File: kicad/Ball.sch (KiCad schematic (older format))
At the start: 32 parts, among them J901 power, K301 G5V-1, Q301 BC547, Q302 BC547, Q303 BC557, Q304 2N3819, Q305 BC547, Q306 2N3819, U301 TL082, U302 TL082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

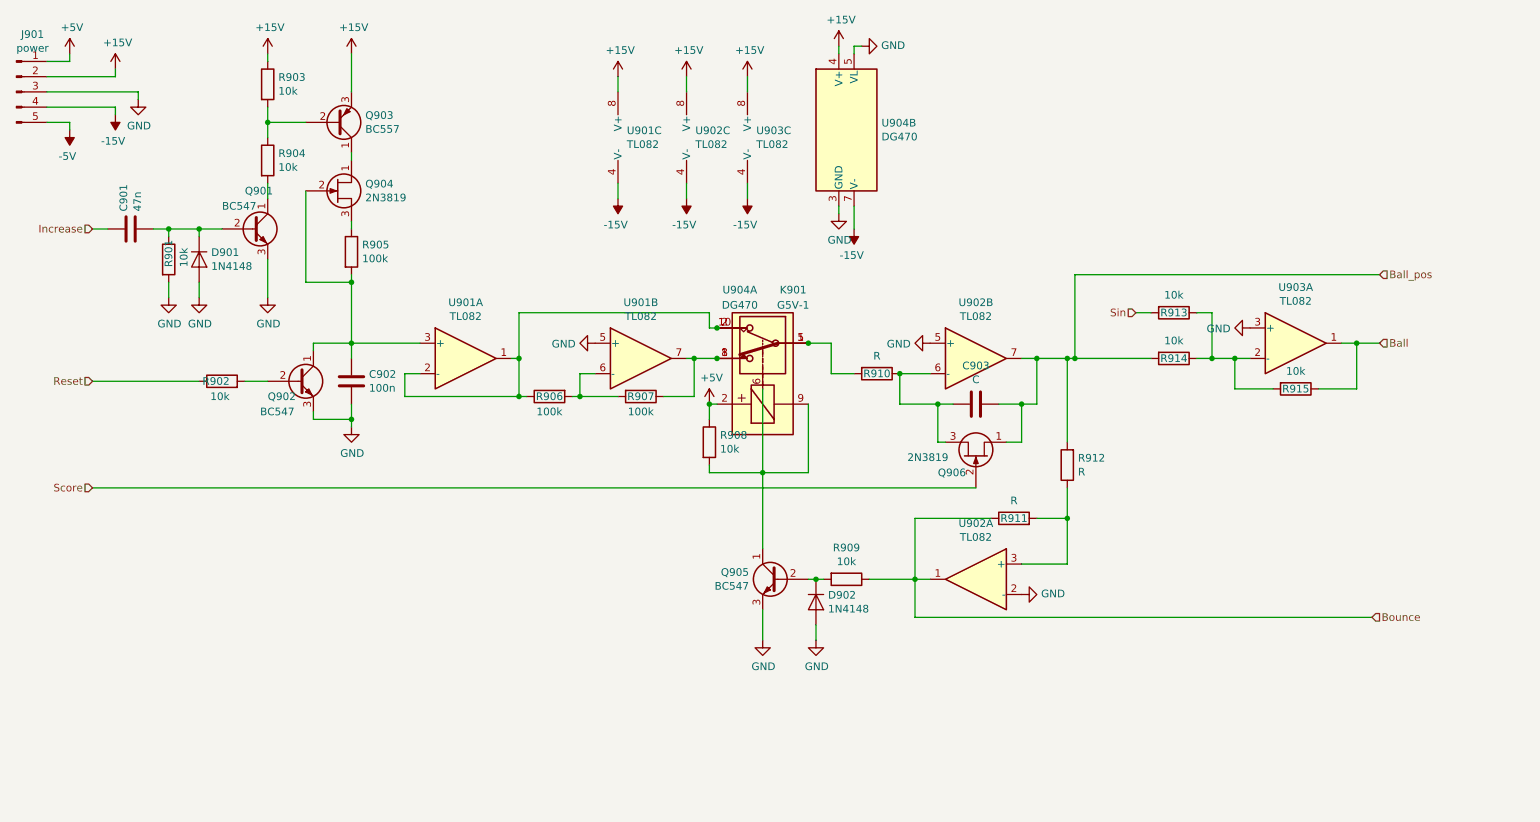
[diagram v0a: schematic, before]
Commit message: Quick fix and documentation
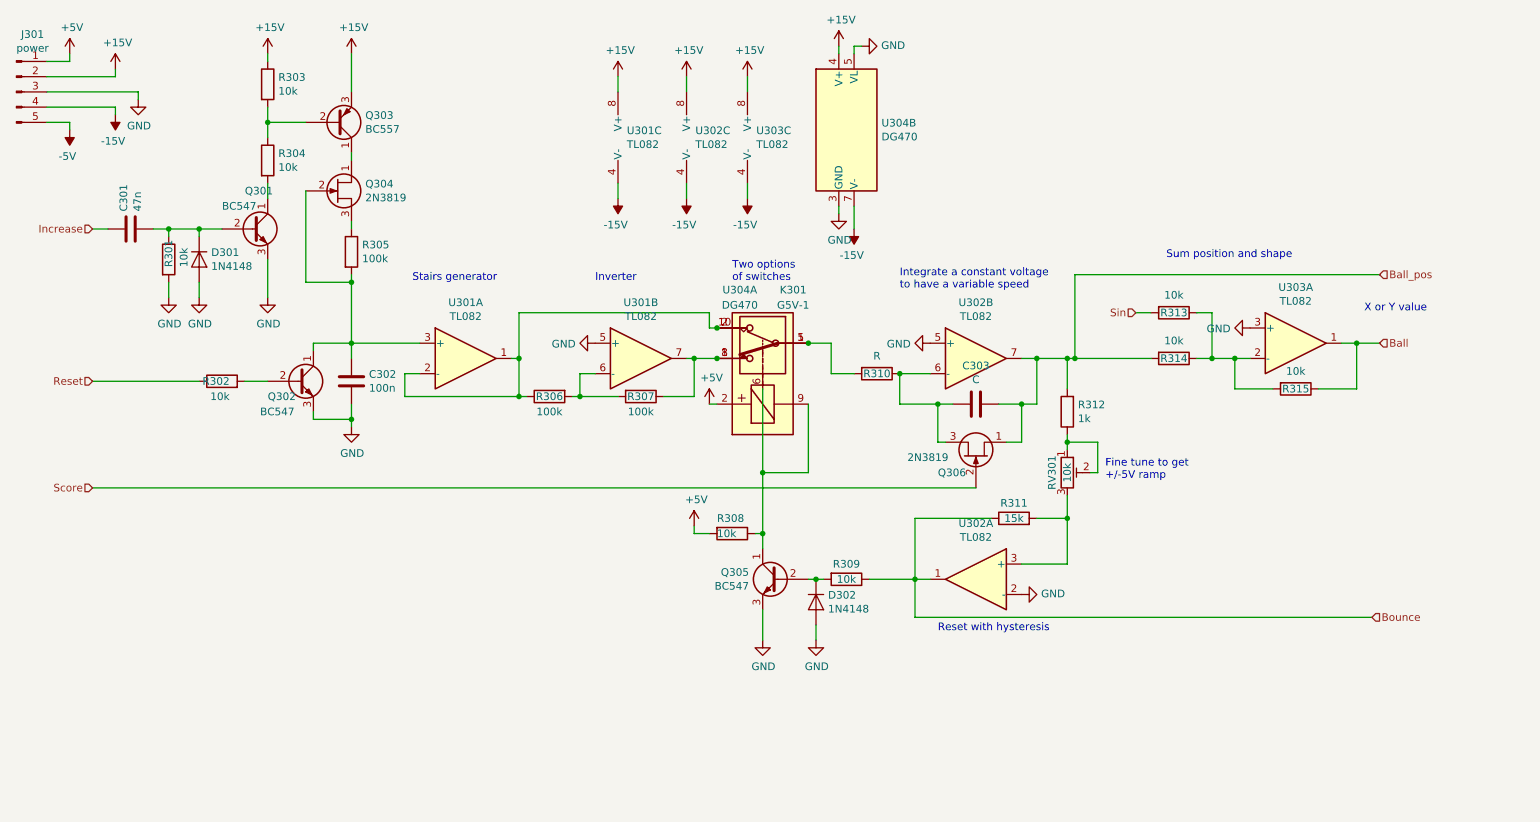
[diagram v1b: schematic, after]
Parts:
- added RV301: 10k, Potentiometer_THT:Potentiometer_Bourns_3299W_Vertical, symbol Device:R_POT_TRIM
- R311: value R -> 15k
- R312: value R -> 1k
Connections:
- net +5V: now also R308.2; no longer R308.1
- net at R311.2, U302.3 (+): now also RV301.3; no longer R312.1
- net at K301.9, Q305.1 (C), U304.6: now also R308.1; no longer R308.2
- new net: R312.1, RV301.1, RV301.2
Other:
- note added: "Fine tune to get\n+/-5V ramp"
- note added: "Integrate a constant voltage\nto have a variable speed"
- note added: "Inverter"
- note added: "Reset with hysteresis"
- note added: "Stairs generator"
- note added: "Sum position and shape"
- note added: "Two options\nof switches"
- note added: "X or Y value"
- moved on the sheet: R308, R312

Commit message: tests and doc ok
still need some scoring options
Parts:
- removed Q306: 2N3819, Package_TO_SOT_THT:TO-92_Inline_Wide, symbol Device:Q_NJFET_DGS
- added U305: DG470, Package_DIP:DIP-8_W7.62mm, symbol Analog_Switch:DG419LDJ
- C301: value 47n -> 470n
- C303: value C -> 10u
- R301: value 10k -> 100k
- R302: value 10k -> 1k
- R310: value R -> 100k
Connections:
- net +15V: now also U305.4 (V+)
- net -15V: now also U305.7 (V-)
- net Ball_pos: now also U305.1
- net GND: now also U305.3 (GND), U305.5 (VL)
- net Score: now also U305.6
- net at C303.1, R310.1, U302.6 (-): now also U305.8
- no-connect marks 0 -> 1
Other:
- note added: "+/-15V output"
- note added: "5V input"
- note added: "LTSPICE - OK"
- moved on the sheet: D302, Q305, R308, R309, R310, R311, R312, RV301, U302A
